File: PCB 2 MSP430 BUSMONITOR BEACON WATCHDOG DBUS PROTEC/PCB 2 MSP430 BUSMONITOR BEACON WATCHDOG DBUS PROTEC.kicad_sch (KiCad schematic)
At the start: 0 parts

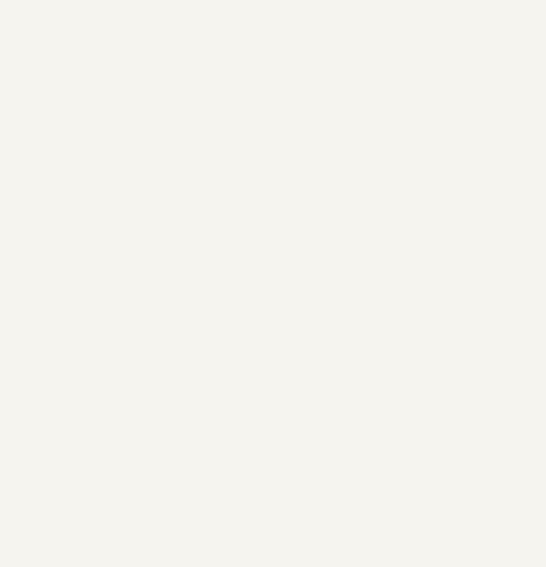
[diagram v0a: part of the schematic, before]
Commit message: Changes
Added bucks from old work
and copied SPV
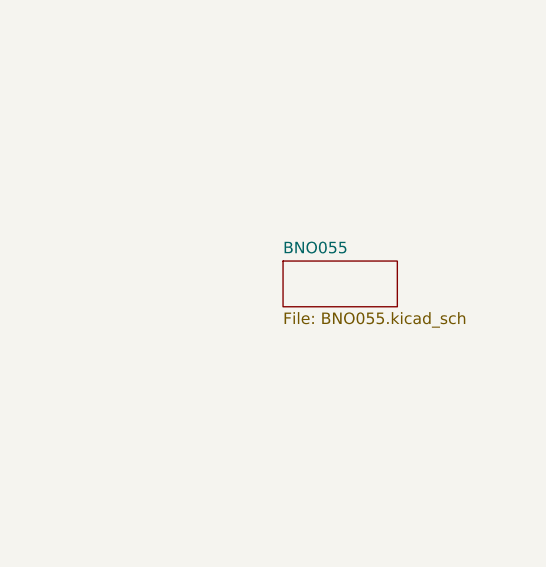
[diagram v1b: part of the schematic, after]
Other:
- added sheet BNO055 (BNO055.kicad_sch)
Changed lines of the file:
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@@
 	(paper "A4")
+	(sheet
+		(at 236.22 73.66)
+		(size 12.7 5.08)
+		(fields_autoplaced yes)
+		(stroke
+			(width 0.1524)
+			(type solid)
+		)
+		(fill
+			(color 0 0 0 0.0000)
+		)
+		(property "Sheetname" "BNO055"
+			(at 236.22 72.9484 0)
+			(effects
+				(font
+					(size 1.27 1.27)
+				)
+				(justify left bottom)
+			)
+		)
+		(property "Sheetfile" "BNO055.kicad_sch"
+			(at 236.22 79.3246 0)
+			(effects
+				(font
+					(size 1.27 1.27)
+				)
+				(justify left top)
+			)
+		)
+		(instances
+			(project "PCB 2 MSP430 BUSMONITOR BEACON WATCHDOG DBUS PROTEC"
+				(path "/04a95c0c-1f2d-49e4-8823-3428ac263eb8"
+					(page "6")
+				)
+			)
+		)
+	)
 	(sheet
 		(at 31.75 48.26)

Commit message: New components
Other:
- added sheet INA219 (INA219.kicad_sch)
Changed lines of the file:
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@@
 	(paper "A4")
 	(sheet
-		(at 236.22 73.66)
-		(size 12.7 5.08)
+		(at 187.96 48.26)
+		(size 16.51 8.89)
 		(fields_autoplaced yes)
 		(stroke
@@
 		)
 		(property "Sheetname" "BNO055"
-			(at 236.22 72.9484 0)
+			(at 187.96 47.5484 0)
 			(effects
 				(font
@@
 		)
 		(property "Sheetfile" "BNO055.kicad_sch"
-			(at 236.22 79.3246 0)
+			(at 187.96 57.7346 0)
 			(effects
 				(font
@@
 	(sheet
 		(at 31.75 48.26)
-		(size 58.42 40.64)
+		(size 14.605 9.525)
 		(fields_autoplaced yes)
 		(stroke
@@
 		)
 		(property "Sheetfile" "MSP430.kicad_sch"
-			(at 31.75 89.4846 0)
+			(at 31.75 58.3696 0)
 			(effects
 				(font
@@
 	(sheet
 		(at 33.02 105.41)
-		(size 60.96 50.8)
+		(size 26.035 18.415)
 		(fields_autoplaced yes)
 		(stroke
@@
 		)
 		(property "Sheetfile" "BEACON.kicad_sch"
-			(at 33.02 156.7946 0)
+			(at 33.02 124.4096 0)
 			(effects
 				(font
@@
 	)
 	(sheet
+		(at 187.96 96.52)
+		(size 36.83 30.48)
+		(fields_autoplaced yes)
+		(stroke
+			(width 0.1524)
+			(type solid)
+		)
+		(fill
+			(color 0 0 0 0.0000)
+		)
+		(property "Sheetname" "INA219"
+			(at 187.96 95.8084 0)
+			(effects
+				(font
+					(size 1.27 1.27)
+				)
+				(justify left bottom)
+			)
+		)
+		(property "Sheetfile" "INA219.kicad_sch"
+			(at 187.96 127.5846 0)
+			(effects
+				(font
+					(size 1.27 1.27)
+				)
+				(justify left top)
+			)
+		)
+		(instances
+			(project "PCB 2 MSP430 BUSMONITOR BEACON WATCHDOG DBUS PROTEC"
+				(path "/04a95c0c-1f2d-49e4-8823-3428ac263eb8"
+					(page "7")
+				)
+			)
+		)
+	)
+	(sheet
 		(at 101.6 105.41)
-		(size 66.04 49.53)
+		(size 31.115 11.43)
 		(fields_autoplaced yes)
 		(stroke
@@
 		)
 		(property "Sheetfile" "DATA_BUS.kicad_sch"
-			(at 101.6 155.5246 0)
+			(at 101.6 117.4246 0)
 			(effects
 				(font
@@
 	(sheet
 		(at 100.33 48.26)
-		(size 66.04 41.91)
+		(size 29.21 13.97)
 		(fields_autoplaced yes)
 		(stroke
@@
 		)
 		(property "Sheetfile" "WATCHDOG.kicad_sch"
-			(at 100.33 90.7546 0)
-			(effects
-				(font
+			(at 100.33 62.8146 0)
+			(effects
+				(font

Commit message: EDITS NTH
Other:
- removed sheet BNO055
- removed sheet INA219
- added sheet LEVEL_SHIFTER (LEVEL_SHIFTER.kicad_sch)
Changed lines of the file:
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@@
 	(paper "A4")
-	(sheet
-		(at 187.96 48.26)
-		(size 16.51 8.89)
-		(fields_autoplaced yes)
-		(stroke
-			(width 0.1524)
-			(type solid)
-		)
-		(fill
-			(color 0 0 0 0.0000)
-		)
-		(property "Sheetname" "BNO055"
-			(at 187.96 47.5484 0)
-			(effects
-				(font
-					(size 1.27 1.27)
-				)
-				(justify left bottom)
-			)
-		)
-		(property "Sheetfile" "BNO055.kicad_sch"
-			(at 187.96 57.7346 0)
-			(effects
-				(font
-					(size 1.27 1.27)
-				)
-				(justify left top)
-			)
-		)
-		(instances
-			(project "PCB 2 MSP430 BUSMONITOR BEACON WATCHDOG DBUS PROTEC"
-				(path "/04a95c0c-1f2d-49e4-8823-3428ac263eb8"
-					(page "6")
-				)
-			)
-		)
-	)
 	(sheet
 		(at 31.75 48.26)
@@
 	)
 	(sheet
+		(at 21.59 149.86)
+		(size 12.7 3.81)
+		(fields_autoplaced yes)
+		(stroke
+			(width 0.1524)
+			(type solid)
+		)
+		(fill
+			(color 0 0 0 0.0000)
+		)
+		(property "Sheetname" "LEVEL_SHIFTER"
+			(at 21.59 149.1484 0)
+			(effects
+				(font
+					(size 1.27 1.27)
+				)
+				(justify left bottom)
+			)
+		)
+		(property "Sheetfile" "LEVEL_SHIFTER.kicad_sch"
+			(at 21.59 154.2546 0)
+			(effects
+				(font
+					(size 1.27 1.27)
+				)
+				(justify left top)
+			)
+		)
+		(instances
+			(project "PCB 2 MSP430 BUSMONITOR BEACON WATCHDOG DBUS PROTEC"
+				(path "/04a95c0c-1f2d-49e4-8823-3428ac263eb8"
+					(page "8")
+				)
+			)
+		)
+	)
+	(sheet
 		(at 33.02 105.41)
 		(size 26.035 18.415)
@@
 				)
 			)
-		)
-	)
-	(sheet
-		(at 187.96 96.52)
-		(size 36.83 30.48)
-		(fields_autoplaced yes)
-		(stroke
-			(width 0.1524)
-			(type solid)
-		)
-		(fill
-			(color 0 0 0 0.0000)
-		)
-		(property "Sheetname" "INA219"
-			(at 187.96 95.8084 0)
-			(effects
-				(font
-					(size 1.27 1.27)
-				)
-				(justify left bottom)
-			)
-		)
-		(property "Sheetfile" "INA219.kicad_sch"
-			(at 187.96 127.5846 0)
-			(effects
-				(font
-					(size 1.27 1.27)
-				)
-				(justify left top)
-			)
-		)
-		(instances
-			(project "PCB 2 MSP430 BUSMONITOR BEACON WATCHDOG DBUS PROTEC"
-				(path "/04a95c0c-1f2d-49e4-8823-3428ac263eb8"
-					(page "7")
-				)
-			)

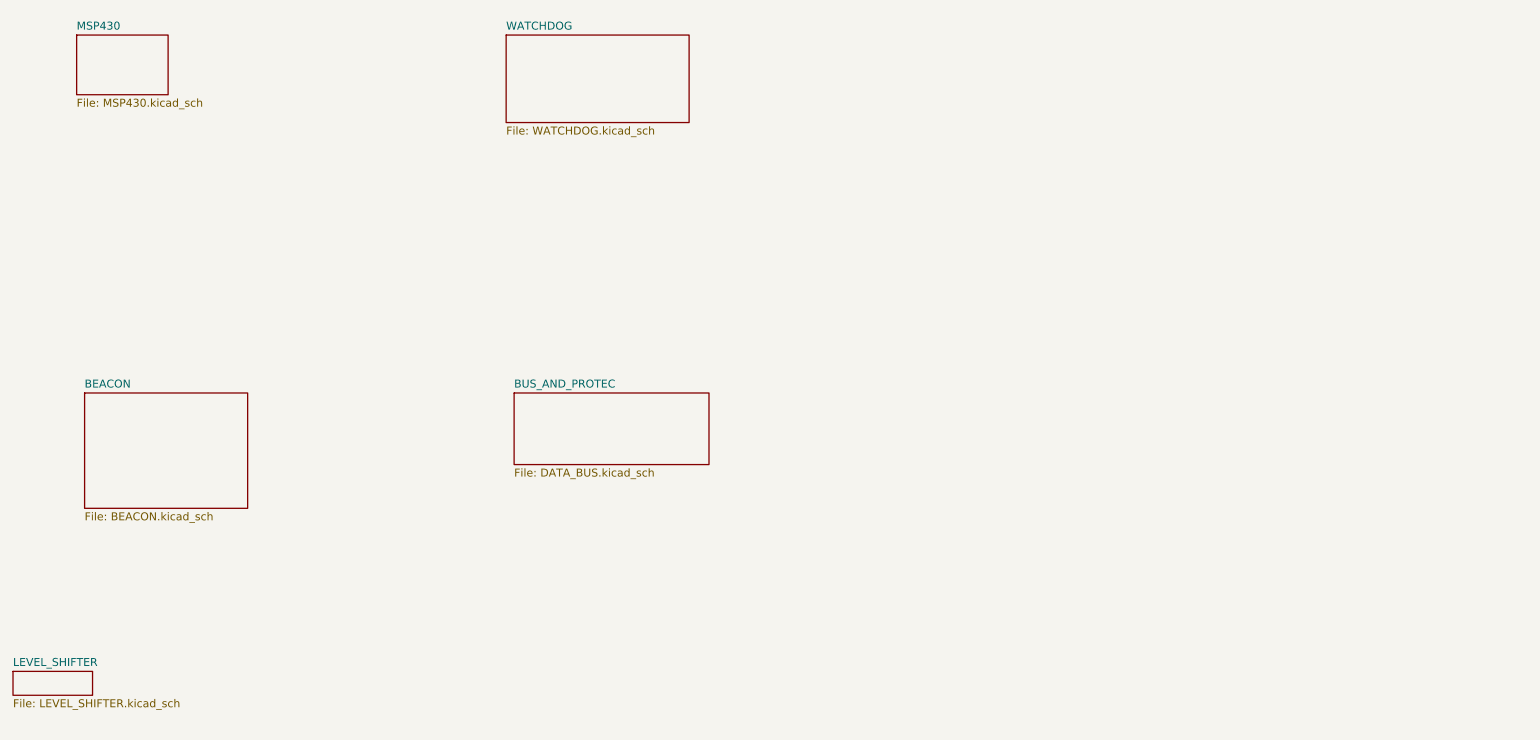
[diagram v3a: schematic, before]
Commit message: Redisgnated components in PCB2 to make more sense
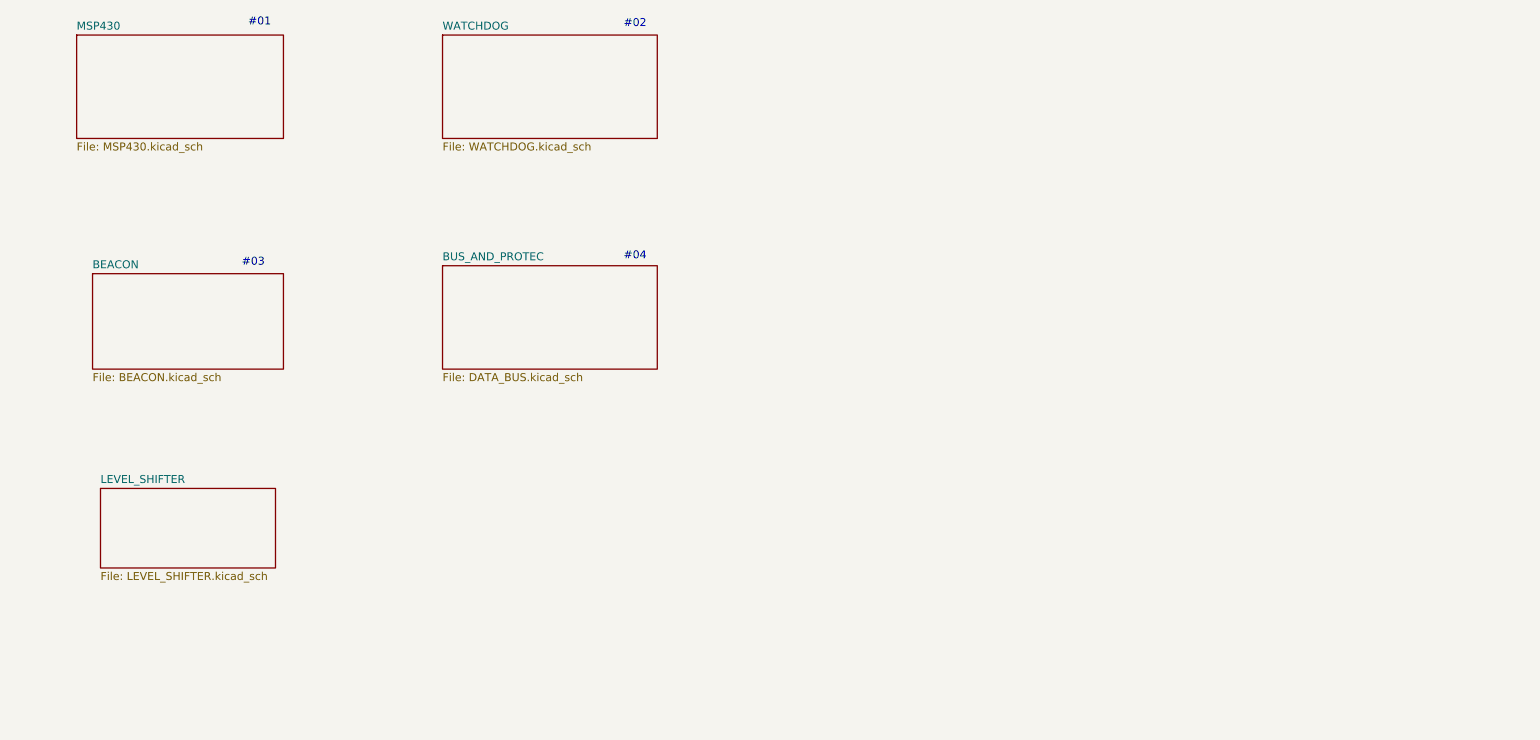
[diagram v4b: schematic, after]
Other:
- note added: "#01"
- note added: "#02"
- note added: "#03"
- note added: "#04"
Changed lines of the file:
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@@
 	(generator_version "8.0")
 	(paper "A4")
+	(text "#03\n"
+		(exclude_from_sim no)
+		(at 59.944 84.582 0)
+		(effects
+			(font
+				(size 1.27 1.27)
+			)
+		)
+	)
+	(text "#01\n"
+		(exclude_from_sim no)
+		(at 60.96 46.228 0)
+		(effects
+			(font
+				(size 1.27 1.27)
+			)
+		)
+	)
+	(text "#04\n"
+		(exclude_from_sim no)
+		(at 120.904 83.566 0)
+		(effects
+			(font
+				(size 1.27 1.27)
+			)
+		)
+	)
+	(text "#02\n"
+		(exclude_from_sim no)
+		(at 120.904 46.482 0)
+		(effects
+			(font
+				(size 1.27 1.27)
+			)
+		)
+	)
 	(sheet
 		(at 31.75 48.26)
-		(size 14.605 9.525)
+		(size 33.02 16.51)
 		(fields_autoplaced yes)
 		(stroke
@@
 		)
 		(property "Sheetfile" "MSP430.kicad_sch"
-			(at 31.75 58.3696 0)
+			(at 31.75 65.3546 0)
 			(effects
 				(font
@@
 	)
 	(sheet
-		(at 21.59 149.86)
-		(size 12.7 3.81)
+		(at 35.56 120.65)
+		(size 27.94 12.7)
 		(fields_autoplaced yes)
 		(stroke
@@
 		)
 		(property "Sheetname" "LEVEL_SHIFTER"
-			(at 21.59 149.1484 0)
+			(at 35.56 119.9384 0)
 			(effects
 				(font
@@
 		)
 		(property "Sheetfile" "LEVEL_SHIFTER.kicad_sch"
-			(at 21.59 154.2546 0)
+			(at 35.56 133.9346 0)
 			(effects
 				(font
@@
 	)
 	(sheet
-		(at 33.02 105.41)
-		(size 26.035 18.415)
+		(at 34.29 86.36)
+		(size 30.48 15.24)
 		(fields_autoplaced yes)
 		(stroke
@@
 		)
 		(property "Sheetname" "BEACON"
-			(at 33.02 104.6984 0)
+			(at 34.29 85.6484 0)
 			(effects
 				(font
@@
 		)
 		(property "Sheetfile" "BEACON.kicad_sch"
-			(at 33.02 124.4096 0)
+			(at 34.29 102.1846 0)
 			(effects
 				(font
@@
 	)
 	(sheet
-		(at 101.6 105.41)
-		(size 31.115 11.43)
+		(at 90.17 85.09)
+		(size 34.29 16.51)
 		(fields_autoplaced yes)
 		(stroke
@@
 		)
 		(property "Sheetname" "BUS_AND_PROTEC"
-			(at 101.6 104.6984 0)
+			(at 90.17 84.3784 0)
 			(effects
 				(font
@@
 		)
 		(property "Sheetfile" "DATA_BUS.kicad_sch"
-			(at 101.6 117.4246 0)
+			(at 90.17 102.1846 0)
 			(effects
 				(font
@@
 		)
 		(property "Field2" ""
-			(at 101.6 105.41 0)
+			(at 90.17 85.09 0)
 			(effects
 				(font
@@
 	)
 	(sheet
-		(at 100.33 48.26)
-		(size 29.21 13.97)
+		(at 90.17 48.26)
+		(size 34.29 16.51)
 		(fields_autoplaced yes)
 		(stroke
@@
 		)
 		(property "Sheetname" "WATCHDOG"
-			(at 100.33 47.5484 0)
+			(at 90.17 47.5484 0)
 			(effects
 				(font
@@
 		)
 		(property "Sheetfile" "WATCHDOG.kicad_sch"
-			(at 100.33 62.8146 0)
-			(effects
-				(font
+			(at 90.17 65.3546 0)
+			(effects
+				(font
